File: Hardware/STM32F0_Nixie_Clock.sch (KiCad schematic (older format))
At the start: 60 parts, among them P101 USB-C Socket, Q101 IRF740S, SW101 Reset, U101 STM32F042F6P6, U102 AMS1117-3.3, U103 DS3231M, U104 MAX1771, U105 HV5222PLCC, U106 HV5222PLCC

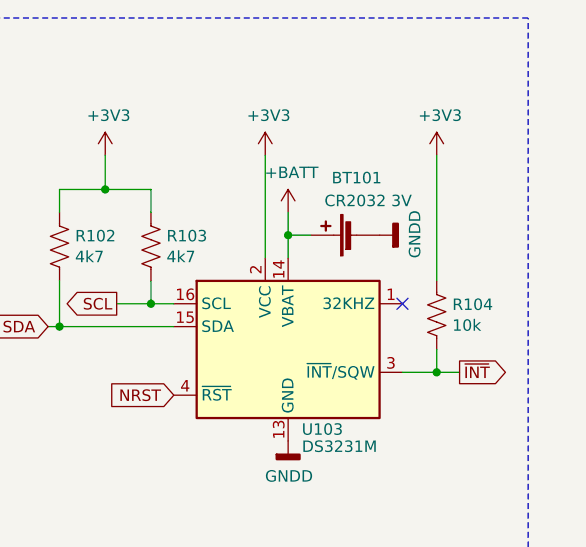
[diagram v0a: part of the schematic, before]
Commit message: Add decoupling decapacitor to RTC
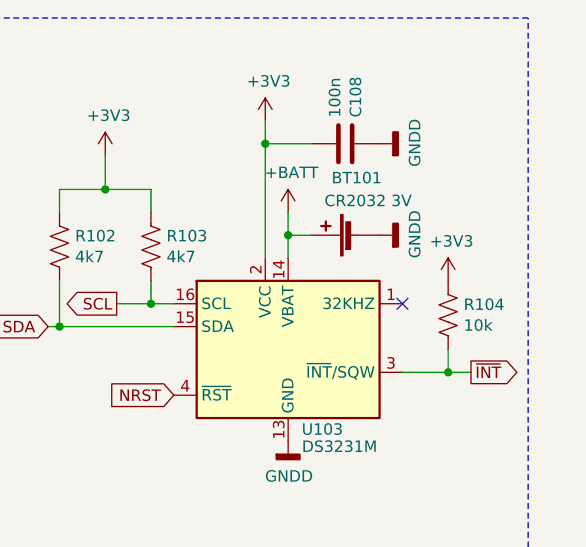
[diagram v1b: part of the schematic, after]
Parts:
- added C108: 100n, Capacitor_SMD:C_0603_1608Metric_Pad1.05x0.95mm_HandSolder, symbol Device:C
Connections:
- net +3V3: now also C108.2
- net GNDA: now also C108.1
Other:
- moved on the sheet: R104
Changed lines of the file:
@@
 Wire Wire Line
 	10050 1550 10150 1550
-Wire Wire Line
-	10550 2150 10700 2150
 $Comp
 L power:GNDD #PWR0109
@@
 L power:+3V3 #PWR0107
 U 1 1 5FE7636B
-P 10700 1200
-F 0 "#PWR0107" H 10700 1050 50  0001 C CNN
-F 1 "+3V3" H 10715 1373 50  0000 C CNN
-F 2 "" H 10700 1200 50  0001 C CNN
-F 3 "" H 10700 1200 50  0001 C CNN
-	1    10700 1200
-	1    0    0    -1
-$EndComp
-Wire Wire Line
-	10700 2150 10800 2150
-Connection ~ 10700 2150
-Wire Wire Line
-	10700 2050 10700 2150
+P 10750 1750
+F 0 "#PWR0107" H 10750 1600 50  0001 C CNN
+F 1 "+3V3" H 10765 1923 50  0000 C CNN
+F 2 "" H 10750 1750 50  0001 C CNN
+F 3 "" H 10750 1750 50  0001 C CNN
+	1    10750 1750
+	1    0    0    -1
+$EndComp
+Wire Wire Line
+	10750 2150 10850 2150
+Connection ~ 10750 2150
+Wire Wire Line
+	10750 2050 10750 2150
 $Comp
 L Device:R_US R104
 U 1 1 5FE6D222
-P 10700 1900
-F 0 "R104" H 10768 1946 50  0000 L CNN
-F 1 "10k" H 10768 1855 50  0000 L CNN
-F 2 "Resistor_SMD:R_0603_1608Metric_Pad1.05x0.95mm_HandSolder" V 10740 1890 50  0001 C CNN
-F 3 "~" H 10700 1900 50  0001 C CNN
-	1    10700 1900
+P 10750 1900
+F 0 "R104" H 10818 1946 50  0000 L CNN
+F 1 "10k" H 10818 1855 50  0000 L CNN
+F 2 "Resistor_SMD:R_0603_1608Metric_Pad1.05x0.95mm_HandSolder" V 10790 1890 50  0001 C CNN
+F 3 "~" H 10750 1900 50  0001 C CNN
+	1    10750 1900
 	1    0    0    -1
 $EndComp
 NoConn ~ 10550 1850
-Text GLabel 10800 2150 2    50   Output ~ 0
+Text GLabel 10850 2150 2    50   Output ~ 0
 ~INT
 $Comp
@@
 L power:+3V3 #PWR0106
 U 1 1 5FDE516F
-P 9950 1200
-F 0 "#PWR0106" H 9950 1050 50  0001 C CNN
-F 1 "+3V3" H 9965 1373 50  0000 C CNN
-F 2 "" H 9950 1200 50  0001 C CNN
-F 3 "" H 9950 1200 50  0001 C CNN
-	1    9950 1200
+P 9950 1050
+F 0 "#PWR0106" H 9950 900 50  0001 C CNN
+F 1 "+3V3" H 9965 1223 50  0000 C CNN
+F 2 "" H 9950 1050 50  0001 C CNN
+F 3 "" H 9950 1050 50  0001 C CNN
+	1    9950 1050
 	1    0    0    -1
 $EndComp
@@
 Wire Wire Line
 	10000 4350 10000 3750
-Wire Wire Line
-	10700 1200 10700 1750
-Wire Wire Line
-	9950 1200 9950 1650
 Wire Wire Line
 	9250 1200 9250 1350
@@
 	1    0    0    -1
 $EndComp
+$Comp
+L Device:C C108
+U 1 1 60145774
+P 10300 1150
+F 0 "C108" H 10415 1196 50  0000 L CNN
+F 1 "100n" H 10415 1105 50  0000 L CNN
+F 2 "Capacitor_SMD:C_0603_1608Metric_Pad1.05x0.95mm_HandSolder" H 10338 1000 50  0001 C CNN
+F 3 "~" H 10300 1150 50  0001 C CNN
+	1    10300 1150
+	0    1    -1   0
+$EndComp
+Wire Wire Line
+	9950 1050 9950 1150
+Wire Wire Line
+	10150 1150 9950 1150
+Connection ~ 9950 1150
+Wire Wire Line
+	9950 1150 9950 1650
+$Comp
+L power:GNDD #PWR0143
+U 1 1 60160AB1
+P 10450 1150
+F 0 "#PWR0143" H 10450 900 50  0001 C CNN
+F 1 "GNDD" H 10454 995 50  0000 C CNN
+F 2 "" H 10450 1150 50  0001 C CNN
+F 3 "" H 10450 1150 50  0001 C CNN
+	1    10450 1150
+	0    -1   -1   0
+$EndComp
+Wire Wire Line
+	10550 2150 10750 2150
 $EndSCHEMATC

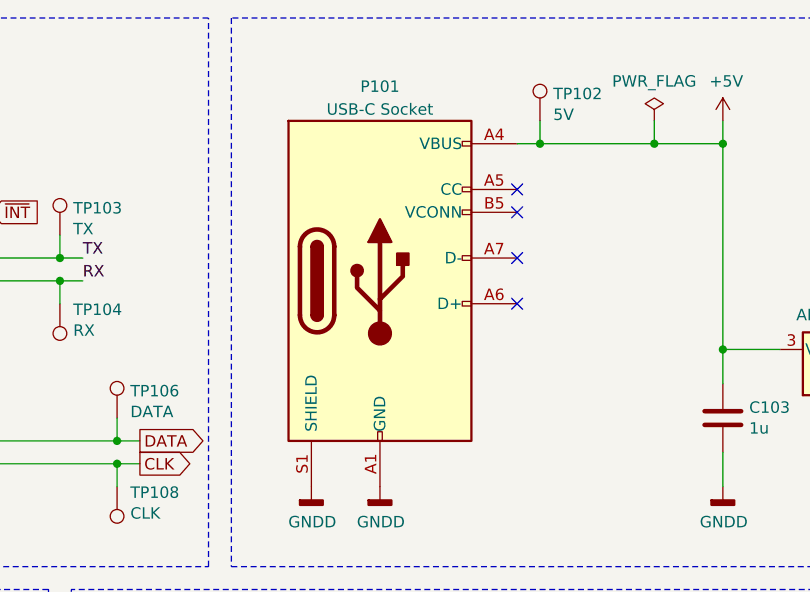
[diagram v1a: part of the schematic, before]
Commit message: Replace USB-C receptacle symbol
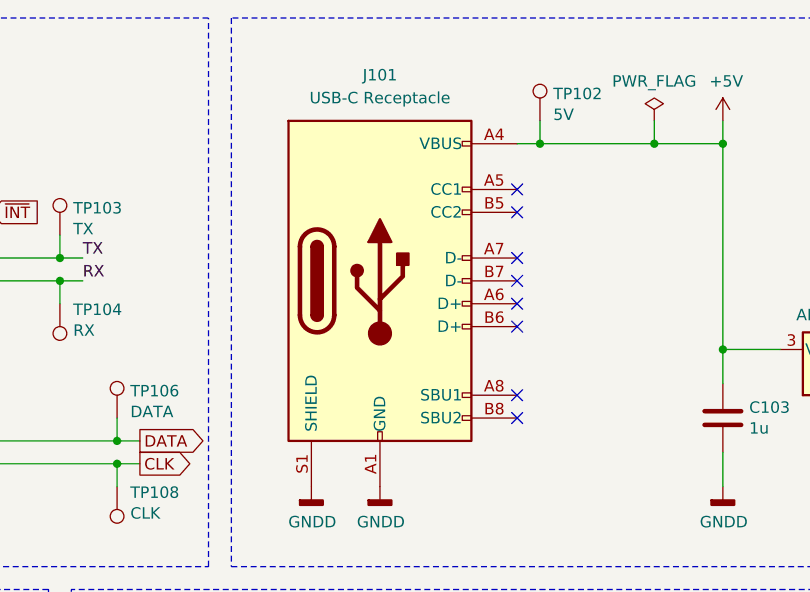
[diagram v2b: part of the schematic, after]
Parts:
- removed P101: USB-C Socket, Connector_USB:USB_C_Receptacle_HRO_TYPE-C-31-M-12, symbol Connector:USB_C_Plug_USB2.0
- added J101: USB-C Receptacle, Connector_USB:USB_C_Receptacle_HRO_TYPE-C-31-M-12, symbol Connector:USB_C_Receptacle_USB2.0
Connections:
- net +5V: now also J101.A4 (VBUS), J101.A9 (VBUS), J101.B4 (VBUS), J101.B9 (VBUS)
- net GNDA: now also J101.A1 (GND), J101.A12 (GND), J101.B1 (GND), J101.B12 (GND), J101.S1 (SHIELD)
- no-connect marks 12 -> 16
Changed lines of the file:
@@
 D4_1
-$Comp
-L Connector:USB_C_Plug_USB2.0 P101
-U 1 1 5FC47AA7
-P 5650 1750
-F 0 "P101" H 5650 2600 50  0000 C CNN
-F 1 "USB-C Socket" H 5650 2500 50  0000 C CNN
-F 2 "Connector_USB:USB_C_Receptacle_HRO_TYPE-C-31-M-12" H 5800 1750 50  0001 C CNN
-F 3 "https://www.usb.org/sites/default/files/documents/usb_type-c.zip" H 5800 1750 50  0001 C CNN
-	1    5650 1750
-	1    0    0    -1
-$EndComp
 $Comp
 L power:GNDD #PWR0115
@@
 Wire Wire Line
 	10550 2150 10750 2150
+$Comp
+L Connector:USB_C_Receptacle_USB2.0 J101
+U 1 1 605F7351
+P 5650 1750
+F 0 "J101" H 5650 2650 50  0000 C CNN
+F 1 "USB-C Receptacle" H 5650 2550 50  0000 C CNN
+F 2 "Connector_USB:USB_C_Receptacle_HRO_TYPE-C-31-M-12" H 5800 1750 50  0001 C CNN
+F 3 "https://www.usb.org/sites/default/files/documents/usb_type-c.zip" H 5800 1750 50  0001 C CNN
+	1    5650 1750
+	1    0    0    -1
+$EndComp
+NoConn ~ 6250 1750
+NoConn ~ 6250 1950
+NoConn ~ 6250 2250
+NoConn ~ 6250 2350
 $EndSCHEMATC
